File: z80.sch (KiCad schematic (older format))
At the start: 0 parts

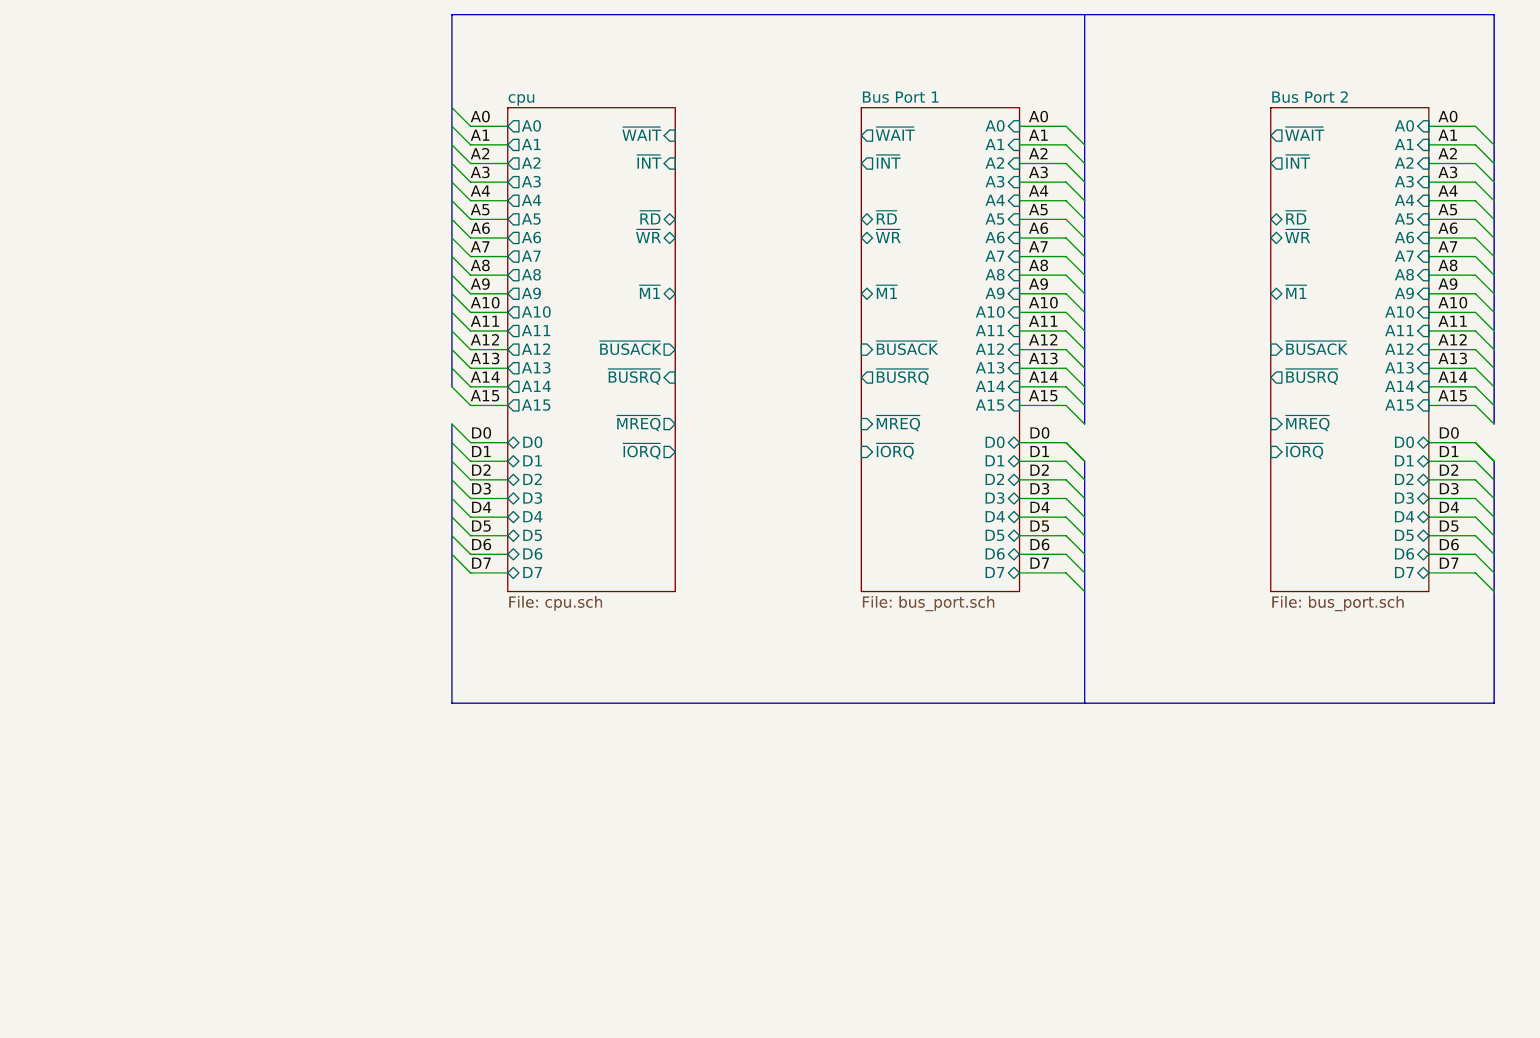
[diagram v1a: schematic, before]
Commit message: More WIP added hierarchical sheets for bus
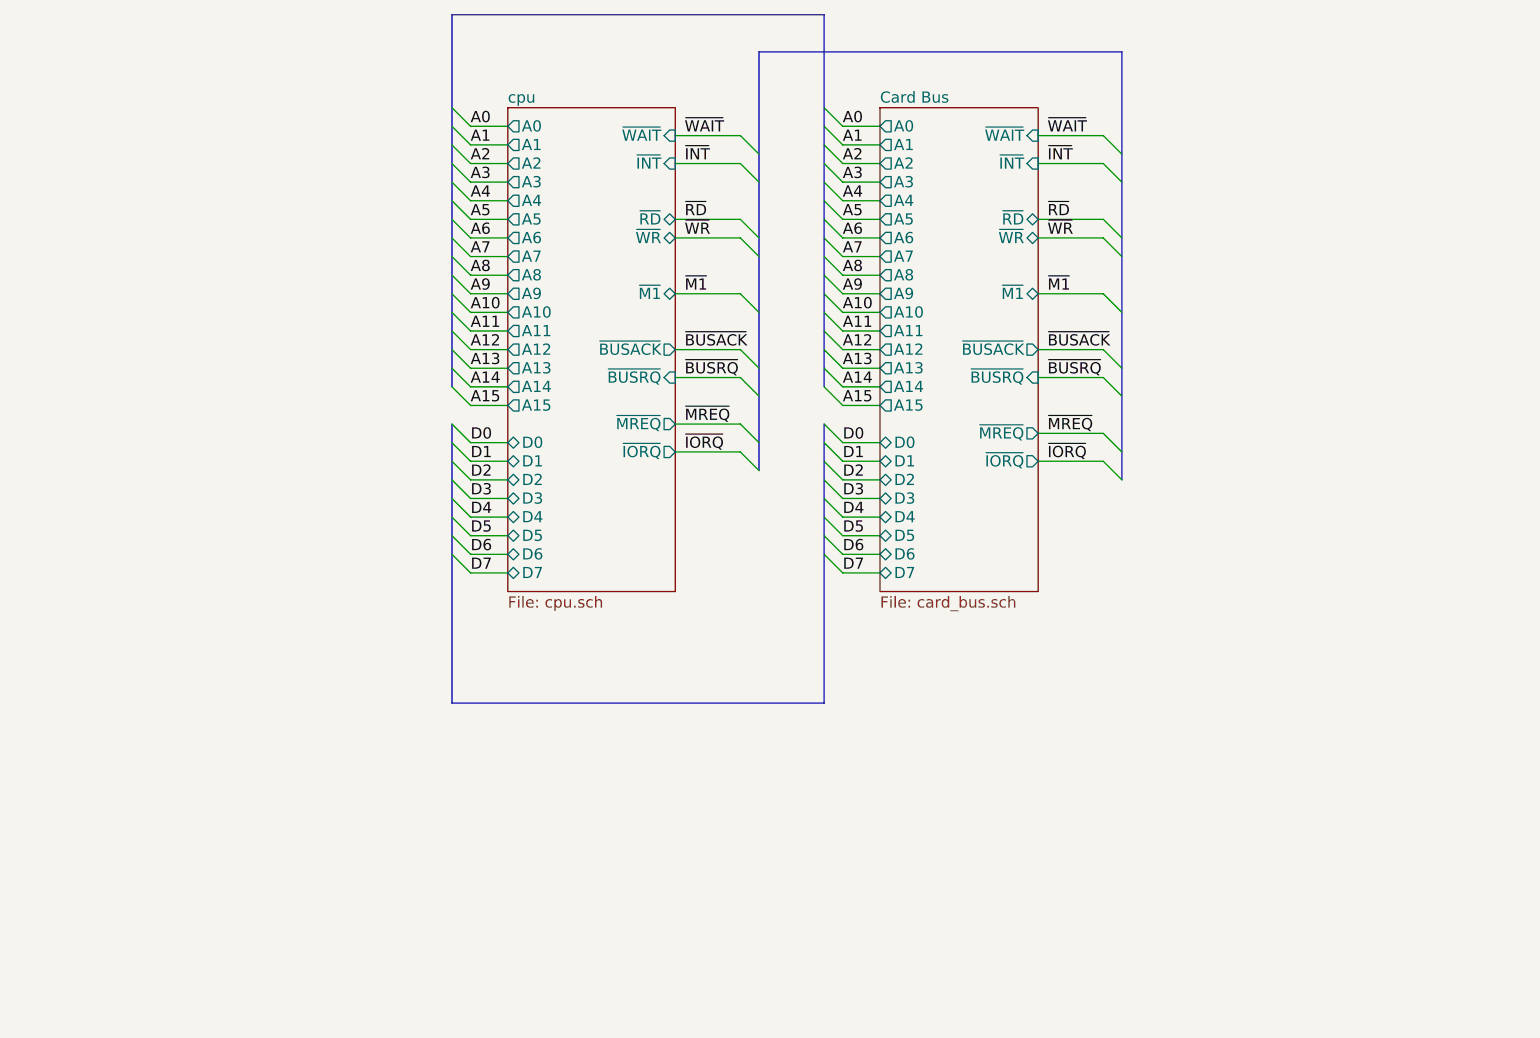
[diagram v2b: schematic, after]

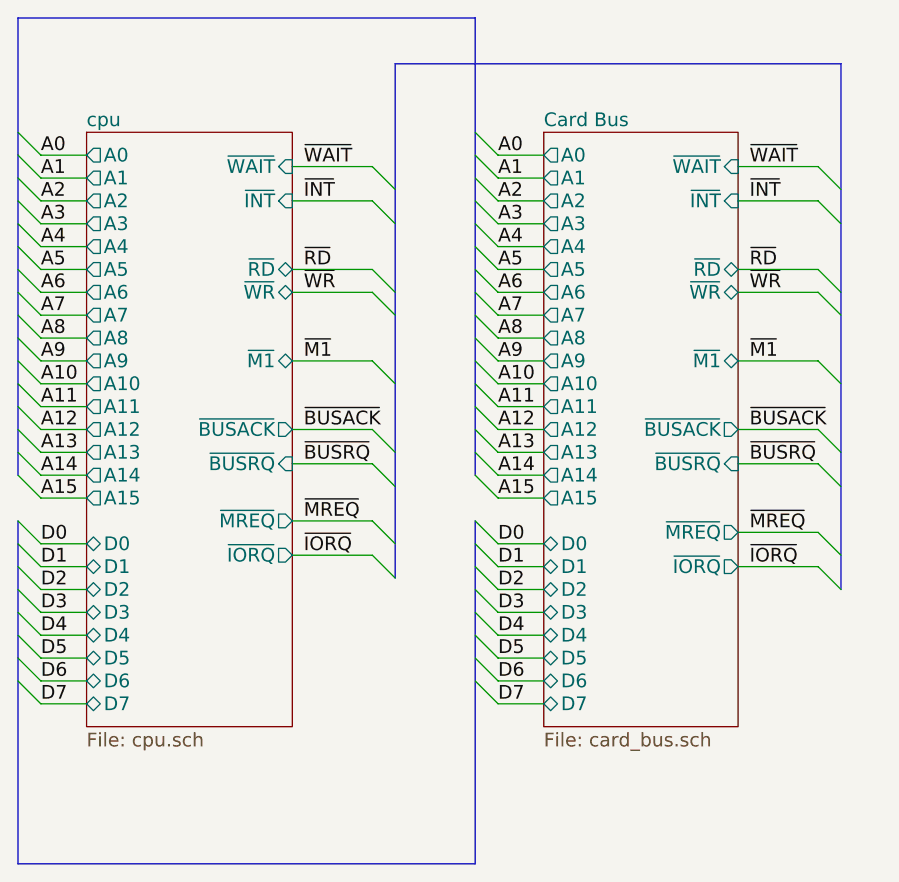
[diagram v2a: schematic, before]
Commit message: Added seperate power pin slots to stop inserting cards backwards
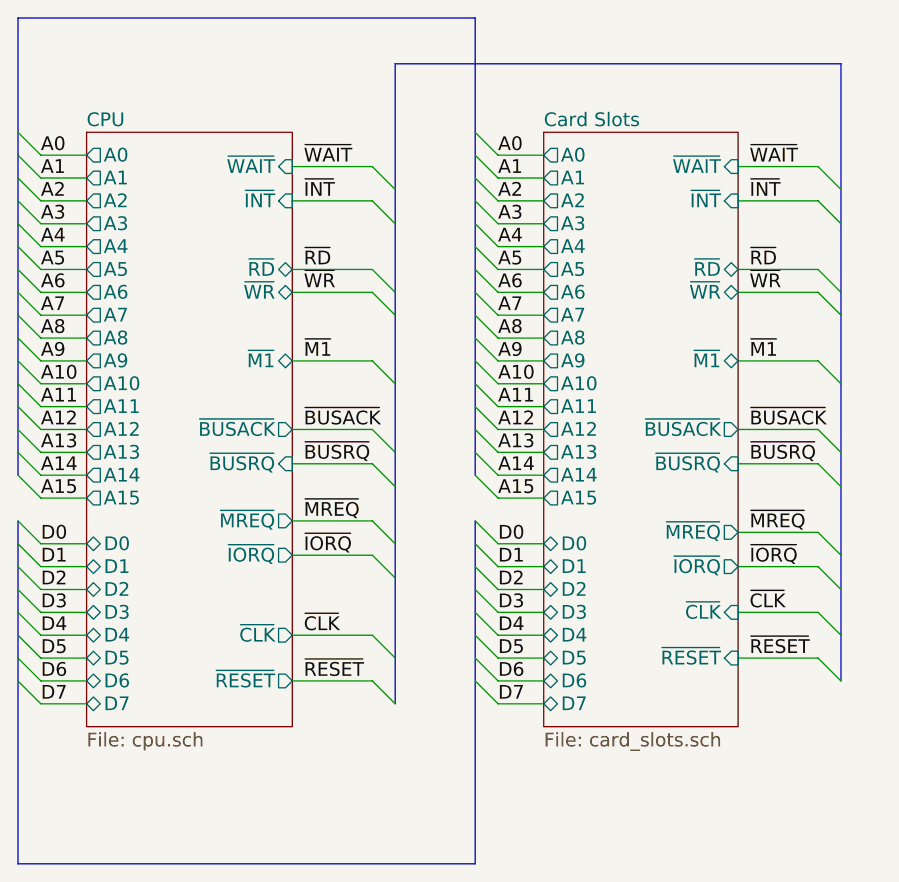
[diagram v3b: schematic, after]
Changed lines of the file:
@@
 S 3600 1400 900  2600
 U 577A9E9B
-F0 "cpu" 60
+F0 "CPU" 60
 F1 "cpu.sch" 60
 F2 "A0" O L 3600 1500 60
@@
 F33 "~MREQ" O R 4500 3100 60
 F34 "~IORQ" O R 4500 3250 60
+F35 "~CLK" O R 4500 3600 60
+F36 "~RESET" O R 4500 3800 60
 $EndSheet
 Text Label 3400 1500 0    60   ~ 0
@@
 S 5600 1400 850  2600
 U 577F17CE
-F0 "Card Bus" 60
-F1 "card_bus.sch" 60
+F0 "Card Slots" 60
+F1 "card_slots.sch" 60
 F2 "A0" O L 5600 1500 60
 F3 "A1" O L 5600 1600 60
@@
 F33 "~MREQ" O R 6450 3150 60
 F34 "~IORQ" O R 6450 3300 60
+F35 "~CLK" I R 6450 3500 60
+F36 "~RESET" I R 6450 3700 60
 $EndSheet
 Text Label 5400 1500 0    60   ~ 0
@@
 ~IORQ
 Wire Bus Line
-	4950 1100 4950 3350
+	4950 1100 4950 3900
 Wire Bus Line
 	4950 1100 6900 1100
@@
 ~IORQ
 Wire Bus Line
-	6900 1100 6900 3400
+	6900 1100 6900 3800
+Wire Wire Line
+	4500 3600 4850 3600
+Wire Wire Line
+	4500 3800 4850 3800
+Text Label 4550 3600 0    60   ~ 0
+~CLK
+Text Label 4550 3800 0    60   ~ 0
+~RESET
+Entry Wire Line
+	4850 3600 4950 3700
+Entry Wire Line
+	4850 3800 4950 3900
+Wire Wire Line
+	6450 3500 6800 3500
+Entry Wire Line
+	6800 3500 6900 3600
+Text Label 6500 3500 0    60   ~ 0
+~CLK
+Wire Wire Line
+	6450 3700 6800 3700
+Entry Wire Line
+	6800 3700 6900 3800
+Text Label 6500 3700 0    60   ~ 0
+~RESET
 $EndSCHEMATC

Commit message: More card slot clean up. Added NMI signal for DMA
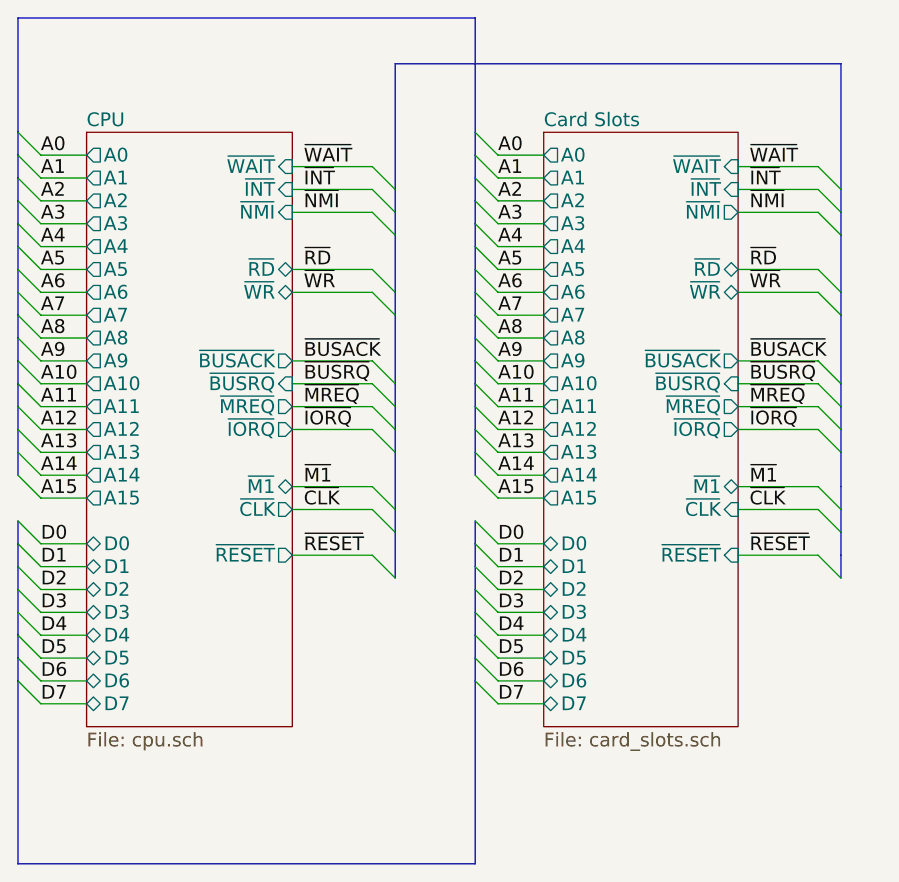
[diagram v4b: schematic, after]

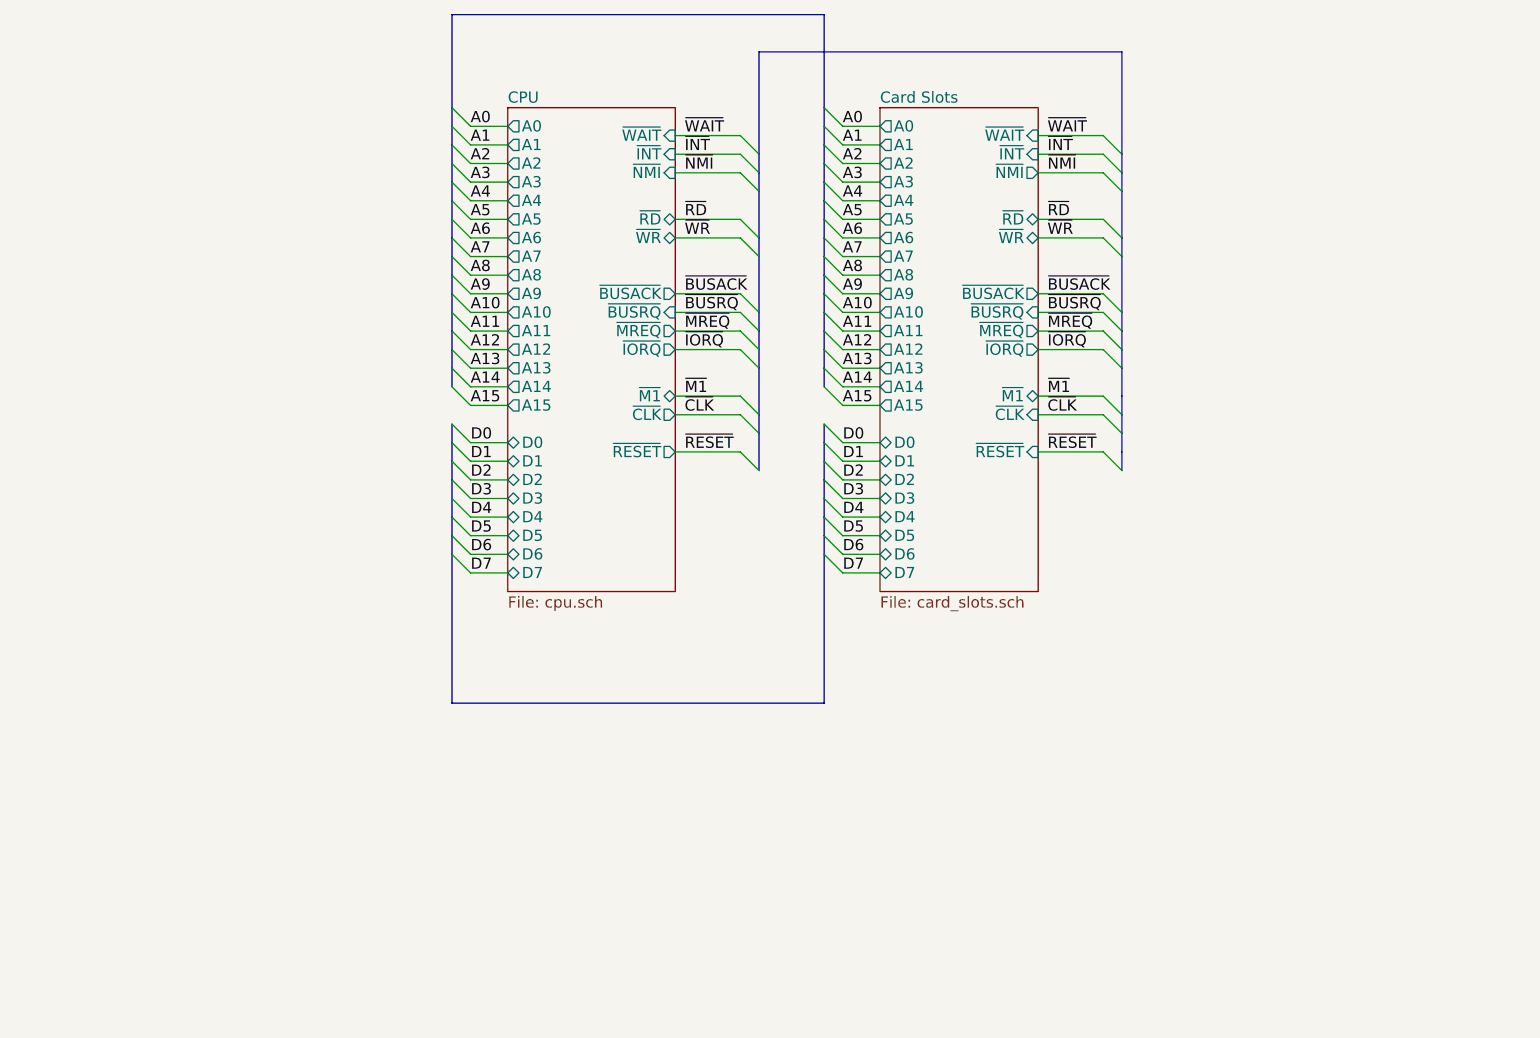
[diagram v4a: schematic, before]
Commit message: Added IO sheet, fixed pin types to match z80
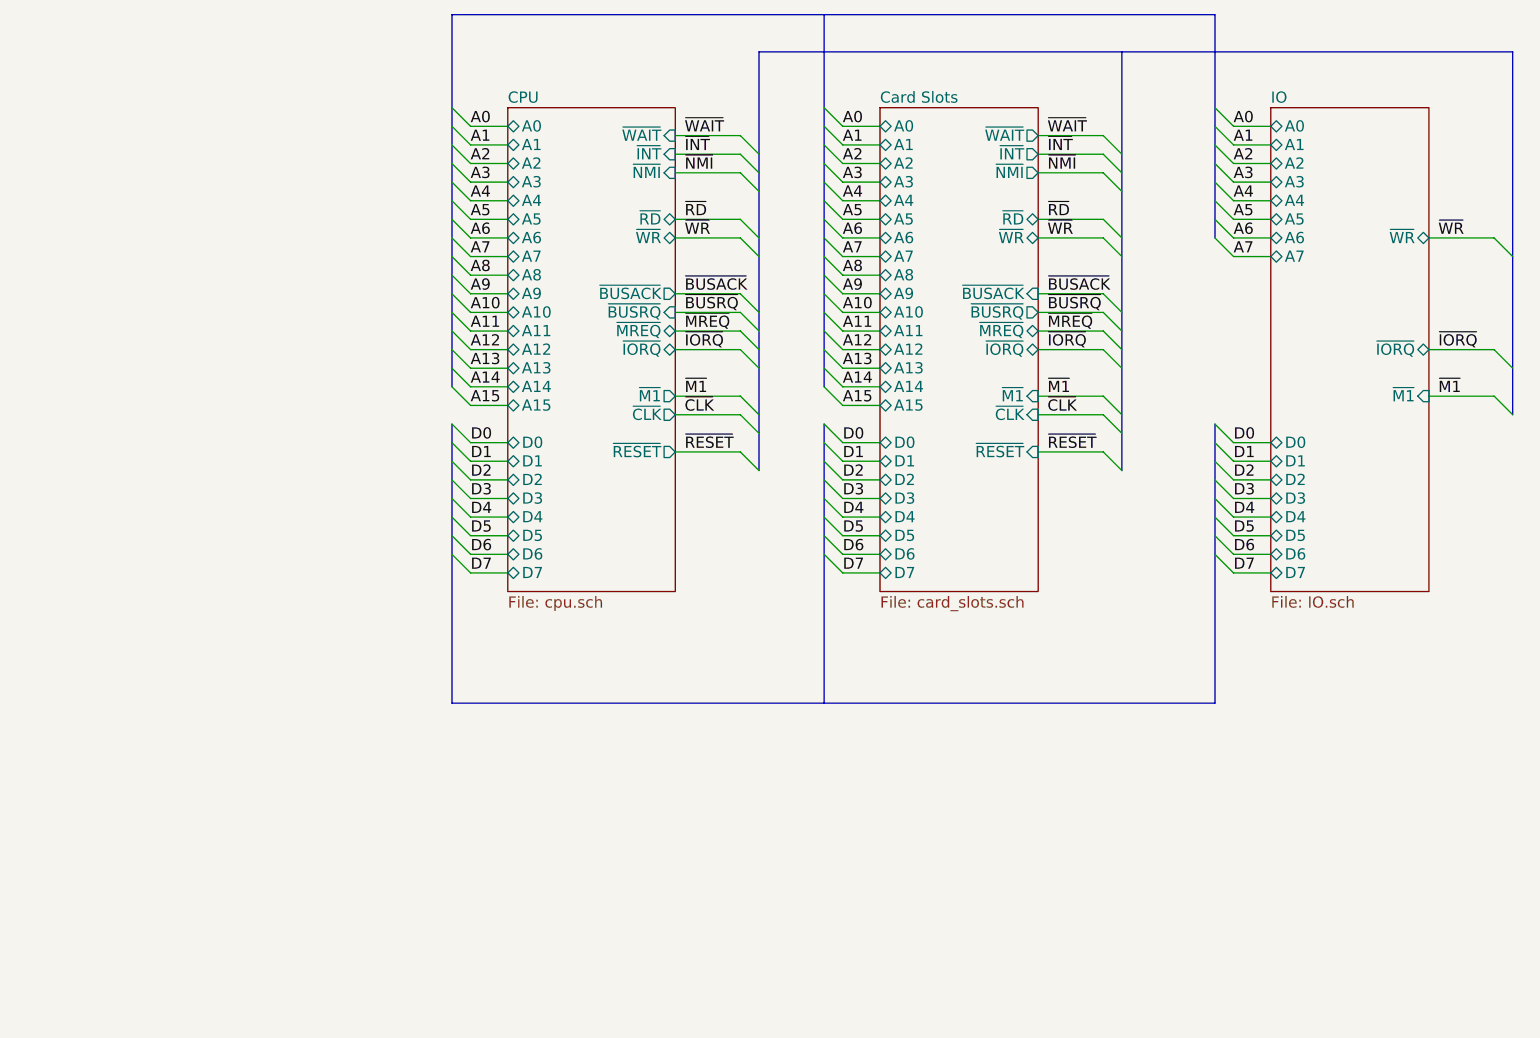
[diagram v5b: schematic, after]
